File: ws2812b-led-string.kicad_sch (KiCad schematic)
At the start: 0 parts

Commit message: nvbghnv bn
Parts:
- added D1: WS2812B, LED_SMD:LED_WS2812B_PLCC4_5.0x5.0mm_P3.2mm, symbol LED:WS2812B
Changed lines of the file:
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@@
 (kicad_sch (version 20230121) (generator eeschema)
   (paper "A4")
+  (symbol (lib_id "LED:WS2812B") (at 127 62.23 0) (unit 1)
+    (in_bom yes) (on_board yes) (dnp no) (fields_autoplaced)
+    (property "Reference" "D1" (at 138.43 59.1059 0)
+      (effects (font (size 1.27 1.27)))
+    )
+    (property "Value" "WS2812B" (at 138.43 61.6459 0)
+      (effects (font (size 1.27 1.27)))
+    )
+    (property "Footprint" "LED_SMD:LED_WS2812B_PLCC4_5.0x5.0mm_P3.2mm" (at 128.27 69.85 0)
+      (effects (font (size 1.27 1.27)) (justify left top) hide)
+    )
+    (property "Datasheet" "https://cdn-shop.adafruit.com/datasheets/WS2812B.pdf" (at 129.54 71.755 0)
+      (effects (font (size 1.27 1.27)) (justify left top) hide)
+    )
+    (pin "1")
+    (pin "2")
+    (pin "3")
+    (pin "4")
+    (instances
+      (project "ImogenWren"
+        (path "/84b7ad53-68b5-40da-9777-f5bb9a09ecb4/257521cf-9b93-4c7d-82f3-71ab472635d5"
+          (reference "D1") (unit 1)
+        )
+      )
+    )
+  )
 )

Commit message: sdfdsfvsd
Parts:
- removed D1: WS2812B, LED_SMD:LED_WS2812B_PLCC4_5.0x5.0mm_P3.2mm, symbol LED:WS2812B
- added C10, C11, C16, C17, C18, C19, C20, C21, C22, C23, C7, C9: 100n, Capacitor_SMD:C_0805_2012Metric_Pad1.18x1.45mm_HandSolder, symbol 000_Capacitor_Film_Immo:cap_film_0805
- added D1, D10, D11, D12, D13, D14, D3, D4, D5, D6, D7, D8: WS2812B, LED_SMD:LED_WS2812B_PLCC4_5.0x5.0mm_P3.2mm, symbol 000_Diodes_Immo:WS2812B
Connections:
- new net: D1.2 (DOUT), D4.4 (DIN)
- new net: D1.4 (DIN), D3.2 (DOUT)
- new net: D4.2 (DOUT), D5.4 (DIN)
- new net: D10.4 (DIN), D8.2 (DOUT)
- new net: D7.2 (DOUT), D8.4 (DIN)
- new net: D13.2 (DOUT), D14.4 (DIN)
- new net: D6.2 (DOUT), D7.4 (DIN)
- new net: D5.2 (DOUT), D6.4 (DIN)
- new net: D11.2 (DOUT), D12.4 (DIN)
- new net: D10.2 (DOUT), D11.4 (DIN)
- new net: D12.2 (DOUT), D13.4 (DIN)
- new net 5V_IN: C10.1, C11.1, C16.1, C17.1, C18.1, C19.1, C20.1, C21.1, C22.1, C23.1, C7.1, C9.1, D1.1 (VDD), D10.1 (VDD), D11.1 (VDD), D12.1 (VDD), D13.1 (VDD), D14.1 (VDD), D3.1 (VDD), D4.1 (VDD), D5.1 (VDD), D6.1 (VDD), D7.1 (VDD), D8.1 (VDD)
- new net DATA_IN: D3.4 (DIN)
- new net DATA_OUT: D14.2 (DOUT)
- new net GND: C10.2, C11.2, C16.2, C17.2, C18.2, C19.2, C20.2, C21.2, C22.2, C23.2, C7.2, C9.2, D1.3 (VSS), D10.3 (VSS), D11.3 (VSS), D12.3 (VSS), D13.3 (VSS), D14.3 (VSS), D3.3 (VSS), D4.3 (VSS), D5.3 (VSS), D6.3 (VSS), D7.3 (VSS), D8.3 (VSS)

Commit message: kjsaofklihsdof
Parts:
- renumbered C7 to C13, C9 to C14, C10 to C15, C11 to C16, C16 to C17, C17 to C18, C18 to C19, C19 to C20, C20 to C21, C21 to C22, C22 to C23, C23 to C24, D3 to WLED1, D12 to WLED10, D13 to WLED11, D14 to WLED12, D1 to WLED2, D4 to WLED3, D5 to WLED4, D6 to WLED5, D7 to WLED6, D8 to WLED7, D10 to WLED8, D11 to WLED9
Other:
- moved on the sheet: C13, C14, C15, C16, C17, C18, C19, C20, C21, C22, C23, C24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

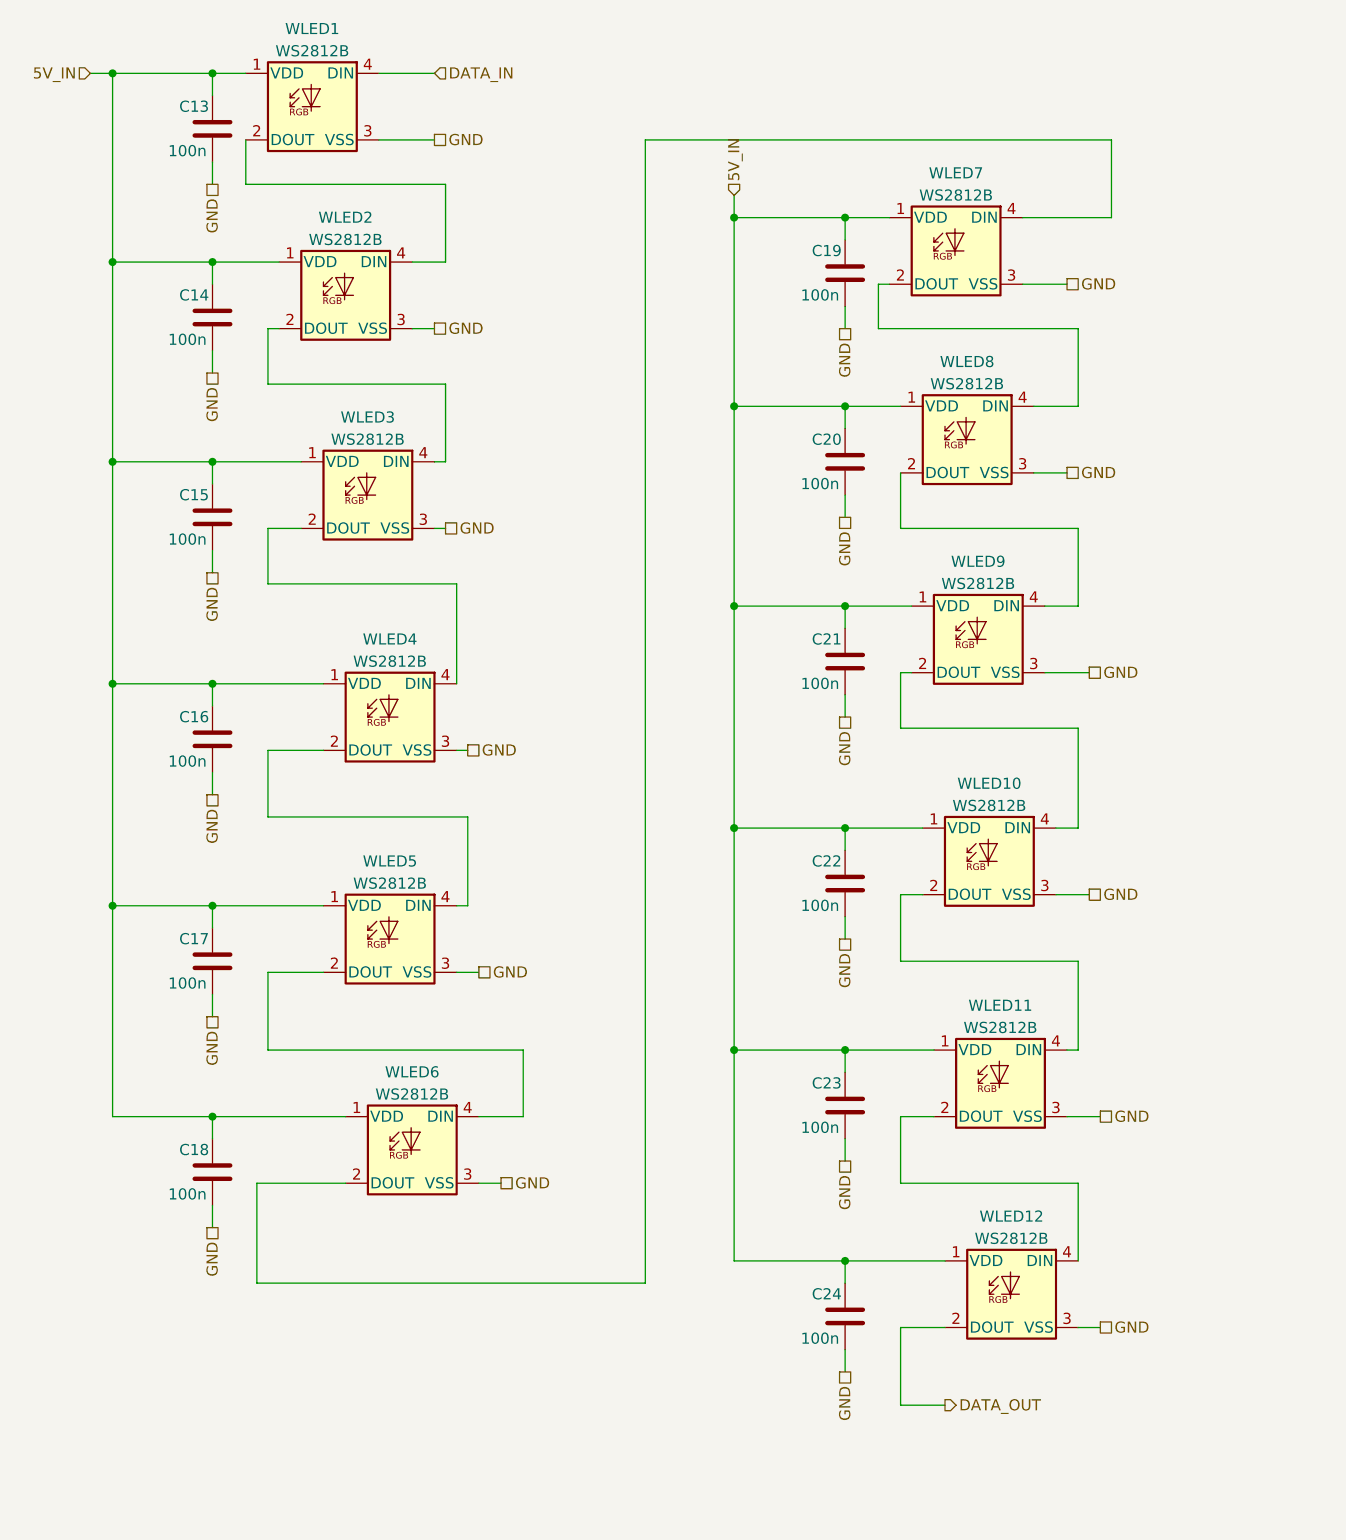
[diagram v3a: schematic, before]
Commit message: Got to Routing. Keeps crashing on me
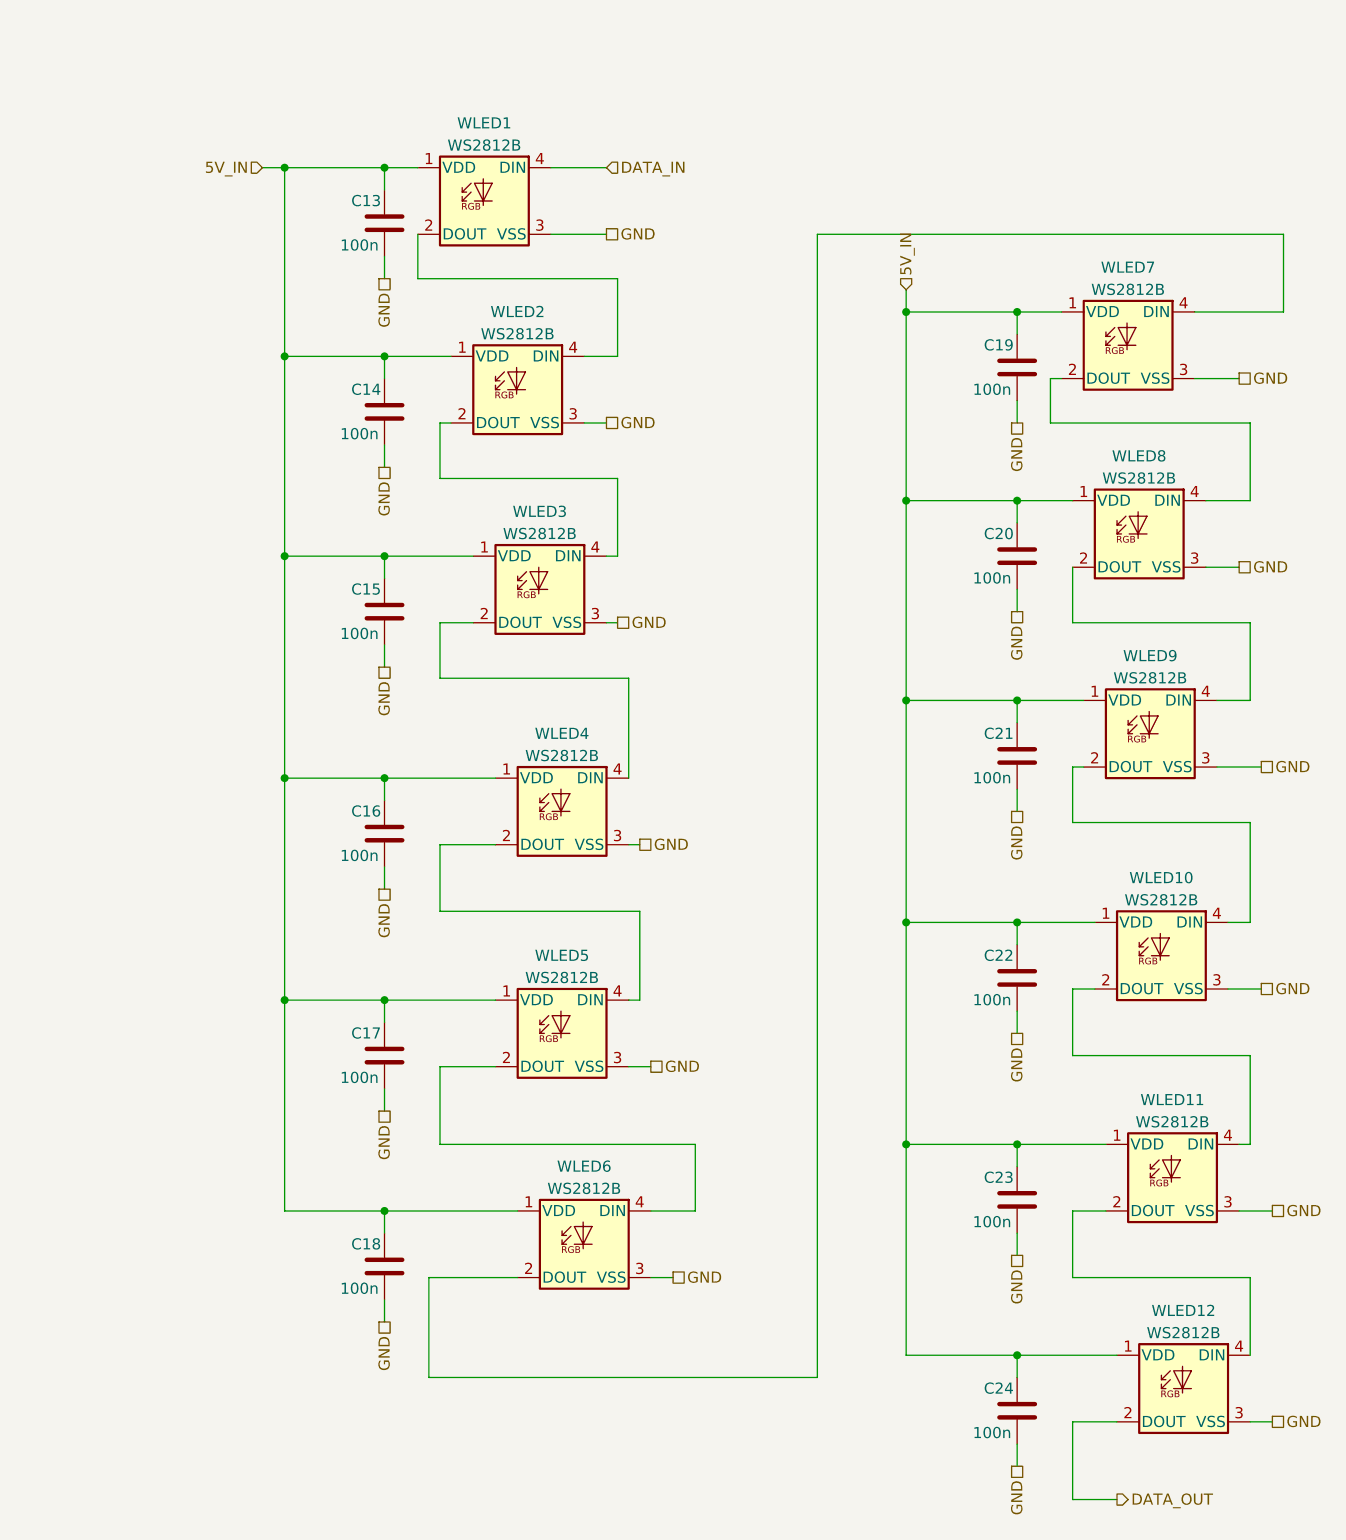
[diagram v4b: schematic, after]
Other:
- moved on the sheet: C13, C14, C15, C16, C17, C18, C19, C20, C21, C22, C23, C24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

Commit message: Adding BOM
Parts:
- C13, C14, C15, C16, C17, C18, C19, C20, C21, C22, C23, C24: footprint Capacitor_SMD:C_0805_2012Metric_Pad1.18x1.45mm_HandSolder -> 000_Capacitors_Immo:C_0805_2012_HandSolder_kawaii; symbol 000_Capacitor_Film_Immo:cap_film_0805 -> 000_Capacitor_Film_Immo:100n; Cost (none) -> 0.02; JLCpart (none) -> C779975
